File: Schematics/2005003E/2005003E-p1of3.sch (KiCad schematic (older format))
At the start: 57 parts, among them Q1 Transistor-NPN, Q2 Transistor-NPN, Q3 Transistor-NPN, Q4 Transistor-NPN, Y1 Crystal

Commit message: Finished filling in the electrical bits in CAD drawing 2005003E, and a lot (but not all yet) of the bill-of-material tabular data.  I found that I hadn't named the various files consistently with the naming convention for the existing schematics, and therefore needed to rename some of them.
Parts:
- added J201: ConnectorB7-600, symbol AGC_DSKY:ConnectorB7-600
- added J202: ConnectorB7-300, symbol AGC_DSKY:ConnectorB7-300
- added J203: ConnectorB7-500, symbol AGC_DSKY:ConnectorB7-500
- added J204: ConnectorB7-100, symbol AGC_DSKY:ConnectorB7-100
- gave numbers to parts that had none: 3
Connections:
- net at C11.2, C3.2, C4.1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: now also R17.2, R18.1, J201.602
- net at C10.1, R1.1: now also J202.302
- net at C10.2, R1.2: now also J201.604
- net at R11.1, R2.1, R3.1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: now also J201.628
- net at R16.2: now also L2.1
- net at R17.1: now also Q1.3 (E)
- net at R10.2, R4.2, R6.1: now also R12.2, J201.629
- net at R5.1: now also J203.502
- net at R13.2: now also J203.503
- net at G1.1: now also J204.169
- net at Q4.1 (C), R27.2: now also J202.304
- net at R25.1, R27.1: now also J203.504
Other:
- note added: "INTERNAL\nTEMPERATURE\nSENSOR"
- note added: "Notes from the Virtual AGC Project:\n1. This CAD drawing was manually transcribed from the original Apollo Program\n document, but is not itself original to the Apollo Program. — RSB 2018\n2. The original drawing did not supply reference designators for the connector to\n the AGC backplane. On this drawing, the numbered oval pads collectively comprise\n connector J1. — RSB 2018"
- note added: "SEE NOTE 3"
- note added: "b"
- note added: "c"
- note added: "e"
- moved on the sheet: R16

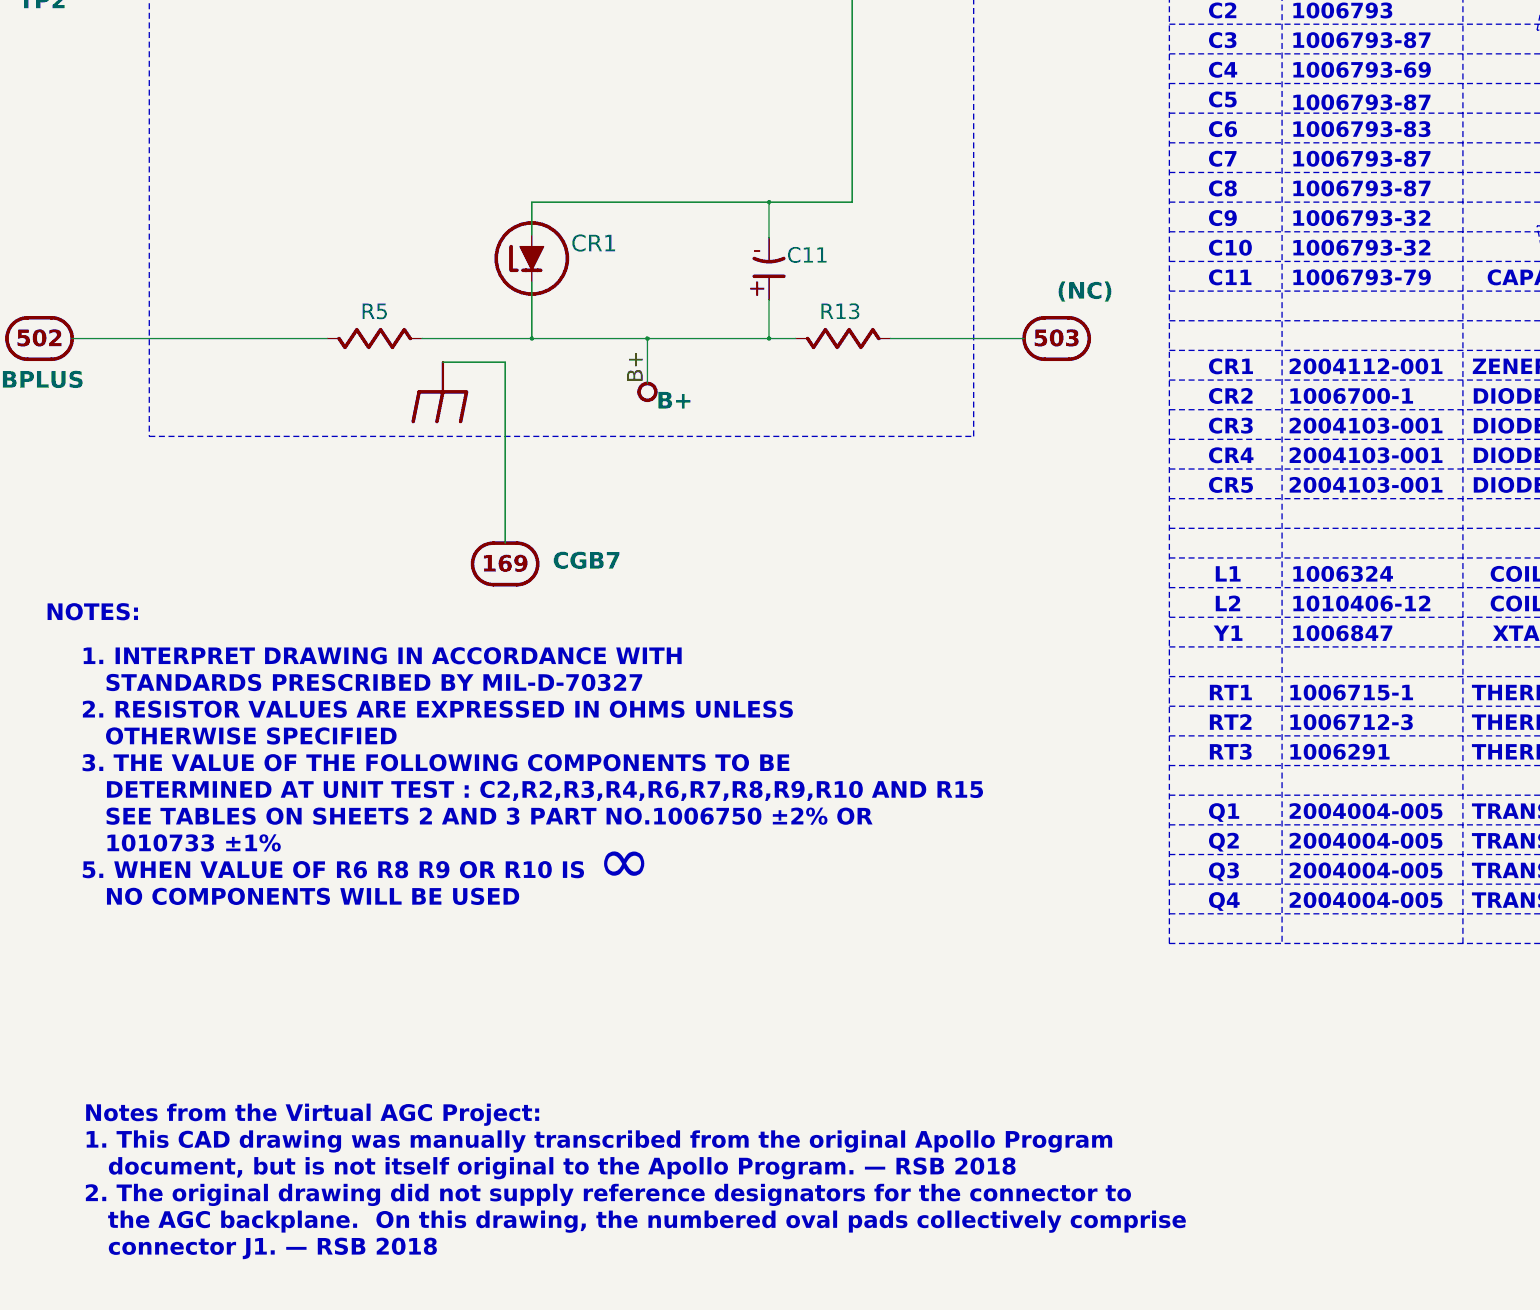
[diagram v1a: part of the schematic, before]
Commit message: Corrected errant connector reference designators and notes.
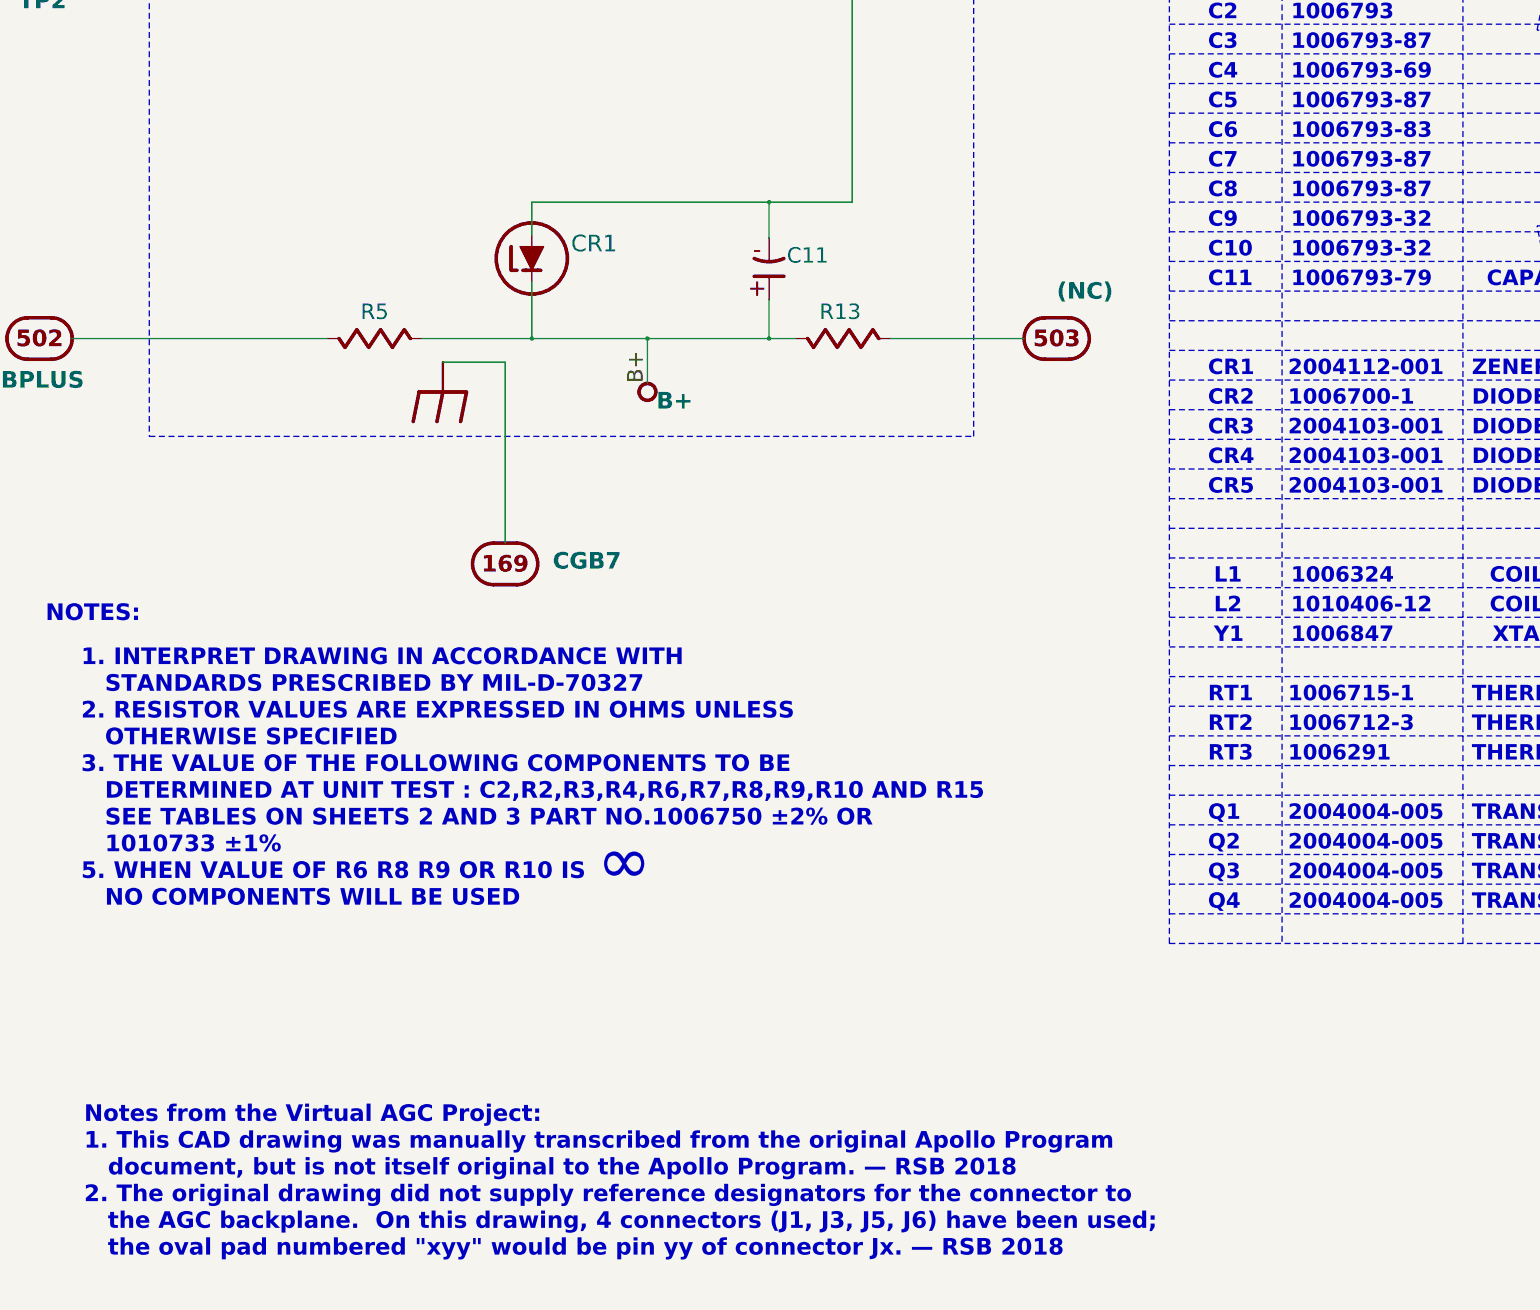
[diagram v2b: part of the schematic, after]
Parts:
- renumbered J204 to J1, J202 to J3, J203 to J5, J201 to J6
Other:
- note added: "Notes from the Virtual AGC Project:\n1. This CAD drawing was manually transcribed from the original Apollo Program\n document, but is not itself original to the Apollo Program. — RSB 2018\n2. The original drawing did not supply reference designators for the connector to\n the AGC backplane. On this drawing, 4 connectors (J1, J3, J5, J6) have been used;\n the oval pad numbered "xyy" would be pin y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"
- note removed: "Notes from the Virtual AGC Project:\n1. This CAD drawing was manually transcribed from the original Apollo Program\n document, but is not itself original to the Apollo Program. — RSB 2018\n2. The original drawing did not supply reference designators for the connector to\n the AGC backplane. On this drawing, the numbered oval pads collectively comprise\n connector J1. — RSB 2018"
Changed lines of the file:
@@
 Text Notes 12075 10975 0    130  ~ 26
 1006793-87
-Text Notes 12075 11500 0    130  ~ 26
+Text Notes 12075 11475 0    130  ~ 26
 1006793-87
 Text Notes 12075 11975 0    130  ~ 26
@@
 ∞
 $Comp
-L AGC_DSKY:ConnectorB7-600 J201
+L AGC_DSKY:ConnectorB7-600 J6
 U 28 1 5BDC2FA6
 P 1475 2800
-F 0 "J201" H 1475 3125 140 0001 C CNN
+F 0 "J6" H 1475 3125 140 0001 C CNN
 F 1 "ConnectorB7-600" H 1475 3225 140 0001 C CNN
 F 2 "" H 1475 2975 140 0001 C CNN
@@
 Connection ~ 3575 2800
 $Comp
-L AGC_DSKY:ConnectorB7-600 J201
+L AGC_DSKY:ConnectorB7-600 J6
 U 29 1 5BDCC662
 P 1550 10250
-F 0 "J201" H 1550 10575 140 0001 C CNN
+F 0 "J6" H 1550 10575 140 0001 C CNN
 F 1 "ConnectorB7-600" H 1550 10675 140 0001 C CNN
 F 2 "" H 1550 10425 140 0001 C CNN
@@
 INTERNAL\nTEMPERATURE\nSENSOR
 $Comp
-L AGC_DSKY:ConnectorB7-600 J201
+L AGC_DSKY:ConnectorB7-600 J6
 U 4 1 5BDD66D6
 P 1500 9225
-F 0 "J201" H 1500 9550 140 0001 C CNN
+F 0 "J6" H 1500 9550 140 0001 C CNN
 F 1 "ConnectorB7-600" H 1500 9650 140 0001 C CNN
 F 2 "" H 1500 9400 140 0001 C CNN
@@
 $EndComp
 $Comp
-L AGC_DSKY:ConnectorB7-300 J202
+L AGC_DSKY:ConnectorB7-300 J3
 U 2 1 5BDD7399
 P 1500 7925
-F 0 "J202" H 1500 8250 140 0001 C CNN
+F 0 "J3" H 1500 8250 140 0001 C CNN
 F 1 "ConnectorB7-300" H 1500 8350 140 0001 C CNN
 F 2 "" H 1500 8100 140 0001 C CNN
@@
 Connection ~ 3025 7925
 $Comp
-L AGC_DSKY:ConnectorB7-500 J203
+L AGC_DSKY:ConnectorB7-500 J5
 U 2 1 5BDEAC7C
 P 1525 13400
-F 0 "J203" H 1525 13725 140 0001 C CNN
+F 0 "J5" H 1525 13725 140 0001 C CNN
 F 1 "ConnectorB7-500" H 1525 13825 140 0001 C CNN
 F 2 "" H 1525 13575 140 0001 C CNN
@@
 	3950 13400 1800 13400
 $Comp
-L AGC_DSKY:ConnectorB7-100 J204
+L AGC_DSKY:ConnectorB7-100 J1
 U 37 2 5BDFE6EE
 P 5450 15300
-F 0 "J204" H 5450 15625 140 0001 C CNN
+F 0 "J1" H 5450 15625 140 0001 C CNN
 F 1 "ConnectorB7-100" H 5450 15725 140 0001 C CNN
 F 2 "" H 5450 15475 140 0001 C CNN
@@
 	5450 13600 5450 15125
 $Comp
-L AGC_DSKY:ConnectorB7-500 J203
+L AGC_DSKY:ConnectorB7-500 J5
 U 3 1 5BE0A321
 P 10100 13400
-F 0 "J203" H 10100 13725 140 0001 C CNN
+F 0 "J5" H 10100 13725 140 0001 C CNN
 F 1 "ConnectorB7-500" H 10100 13825 140 0001 C CNN
 F 2 "" H 10100 13575 140 0001 C CNN
@@
 SEE NOTE 3
 $Comp
-L AGC_DSKY:ConnectorB7-500 J203
+L AGC_DSKY:ConnectorB7-500 J5
 U 4 1 5BE14E67
 P 24250 2375
-F 0 "J203" H 24250 2700 140 0001 C CNN
+F 0 "J5" H 24250 2700 140 0001 C CNN
 F 1 "ConnectorB7-500" H 24250 2800 140 0001 C CNN
 F 2 "" H 24250 2550 140 0001 C CNN
@@
 Connection ~ 19800 2375
 $Comp
-L AGC_DSKY:ConnectorB7-300 J202
+L AGC_DSKY:ConnectorB7-300 J3
 U 4 1 5BE291F7
 P 24250 3400
-F 0 "J202" H 24250 3725 140 0001 C CNN
+F 0 "J3" H 24250 3725 140 0001 C CNN
 F 1 "ConnectorB7-300" H 24250 3825 140 0001 C CNN
 F 2 "" H 24250 3575 140 0001 C CNN
@@
 	19800 3400 19800 3700
 $Comp
-L AGC_DSKY:ConnectorB7-600 J201
+L AGC_DSKY:ConnectorB7-600 J6
 U 2 1 5BE336F1
 P 24275 7225
-F 0 "J201" H 24275 7550 140 0001 C CNN
+F 0 "J6" H 24275 7550 140 0001 C CNN
 F 1 "ConnectorB7-600" H 24275 7650 140 0001 C CNN
 F 2 "" H 24275 7400 140 0001 C CNN
@@
 	11100 7200 11100 7225
 Text Notes 1900 21150 0    140  ~ 28
-Notes from the Virtual AGC Project:\n1. This CAD drawing was manually transcribed from the original Apollo Program\n   document, but is not itself original to the Apollo Program. — RSB 2018\n2. The original drawing did not supply reference designators for the connector to\n   the AGC backplane.  On this drawing, the numbered oval pads collectively comprise\n   connector J1. — RSB 2018
+Notes from the Virtual AGC Project:\n1. This CAD drawing was manually transcribed from the original Apollo Program\n   document, but is not itself original to the Apollo Program. — RSB 2018\n2. The original drawing did not supply reference designators for the connector to\n   the AGC backplane.  On this drawing, 4 connectors (J1, J3, J5, J6) have been used;\n   the oval pad numbered "xyy" would be pin yy of connector Jx. — RSB 2018
 $Bitmap
 Pos 1600 19975
